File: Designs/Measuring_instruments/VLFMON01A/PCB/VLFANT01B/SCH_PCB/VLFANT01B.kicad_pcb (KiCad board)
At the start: 2 copper layers, 50.3 x 40.1 mm, 9 parts, among them J1 RJ45_RJHSE-5384, J2 RJ45_RJHSE-5384, J3 RJ45_RJHSE-5384, J7 SMA, J9 JUMP_3X2, M1 HOLE, M2 HOLE, M3 HOLE, M4 HOLE

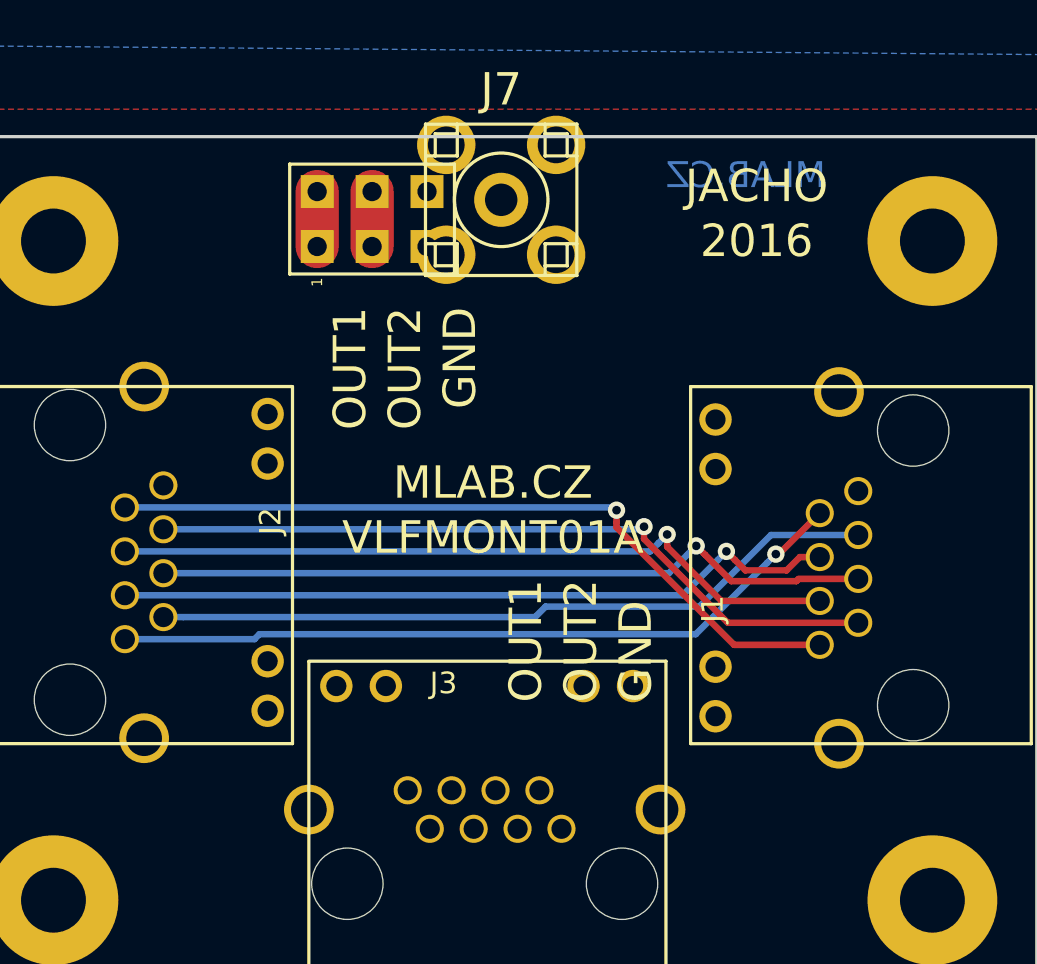
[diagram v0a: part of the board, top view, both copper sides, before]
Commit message: 
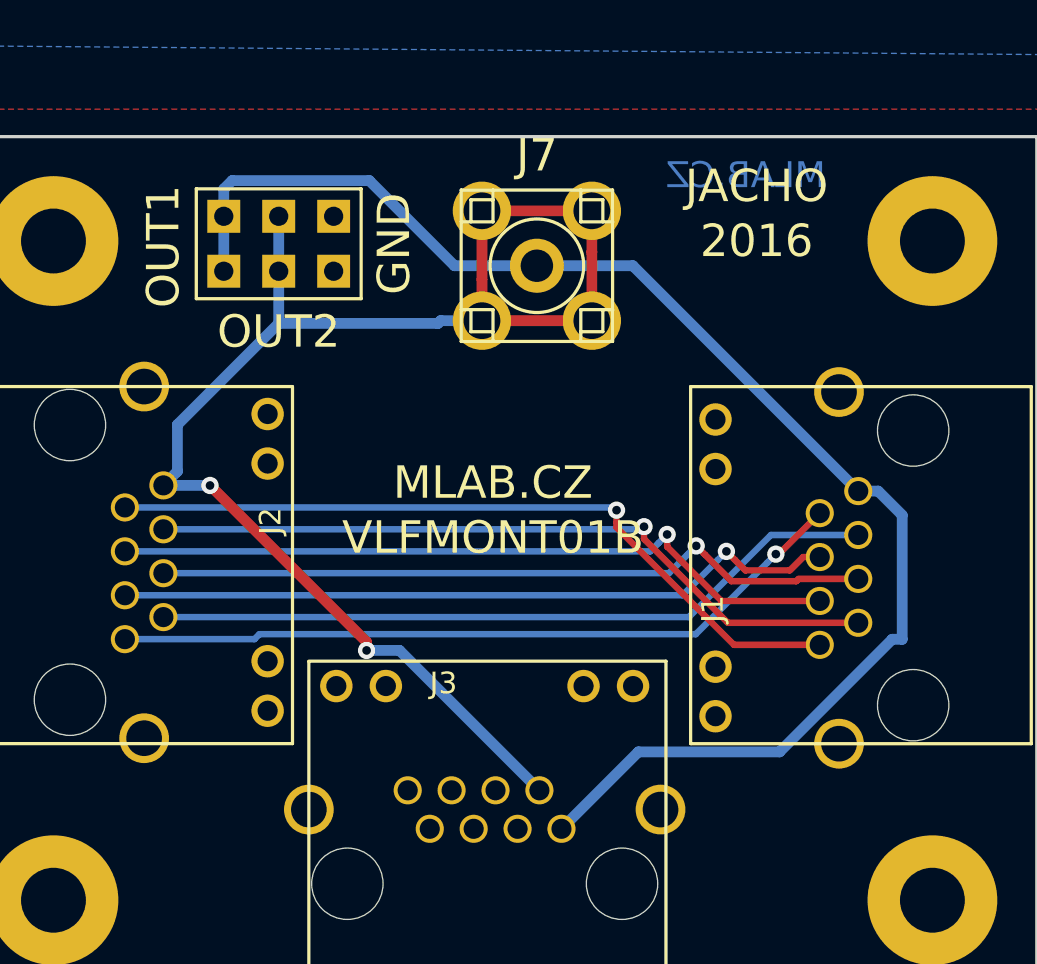
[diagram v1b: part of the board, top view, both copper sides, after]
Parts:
- moved J9 4.47 mm to (15.5, -35.4)
- moved J7 3.47 mm to (27.4, -34.4)
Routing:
- net /OUT2: track 2.54 -> 67.9 mm, vias 0 -> 2
- net /OUT1: track 2.54 -> 66.9 mm
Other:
- board text added: "VLFMONT01B"
- board text removed: "VLFMONT01A"

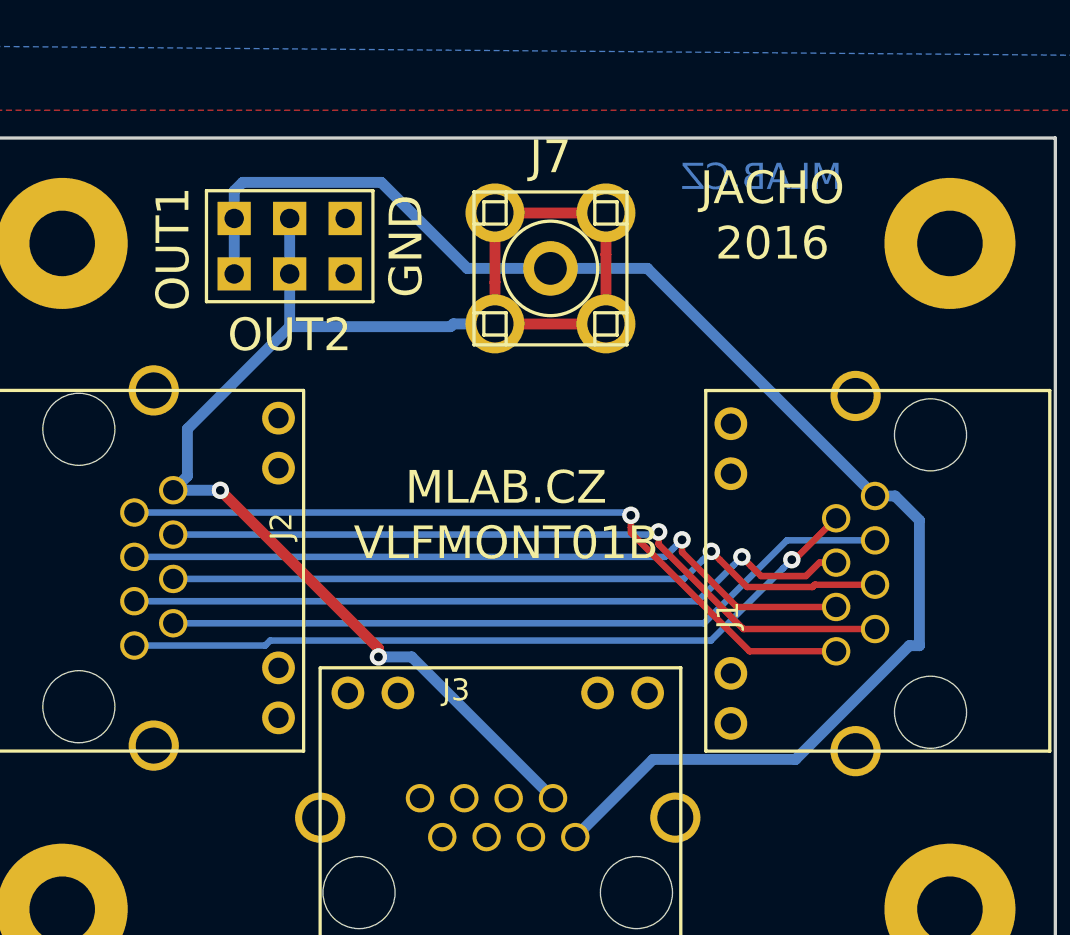
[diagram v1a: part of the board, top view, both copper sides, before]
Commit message: 
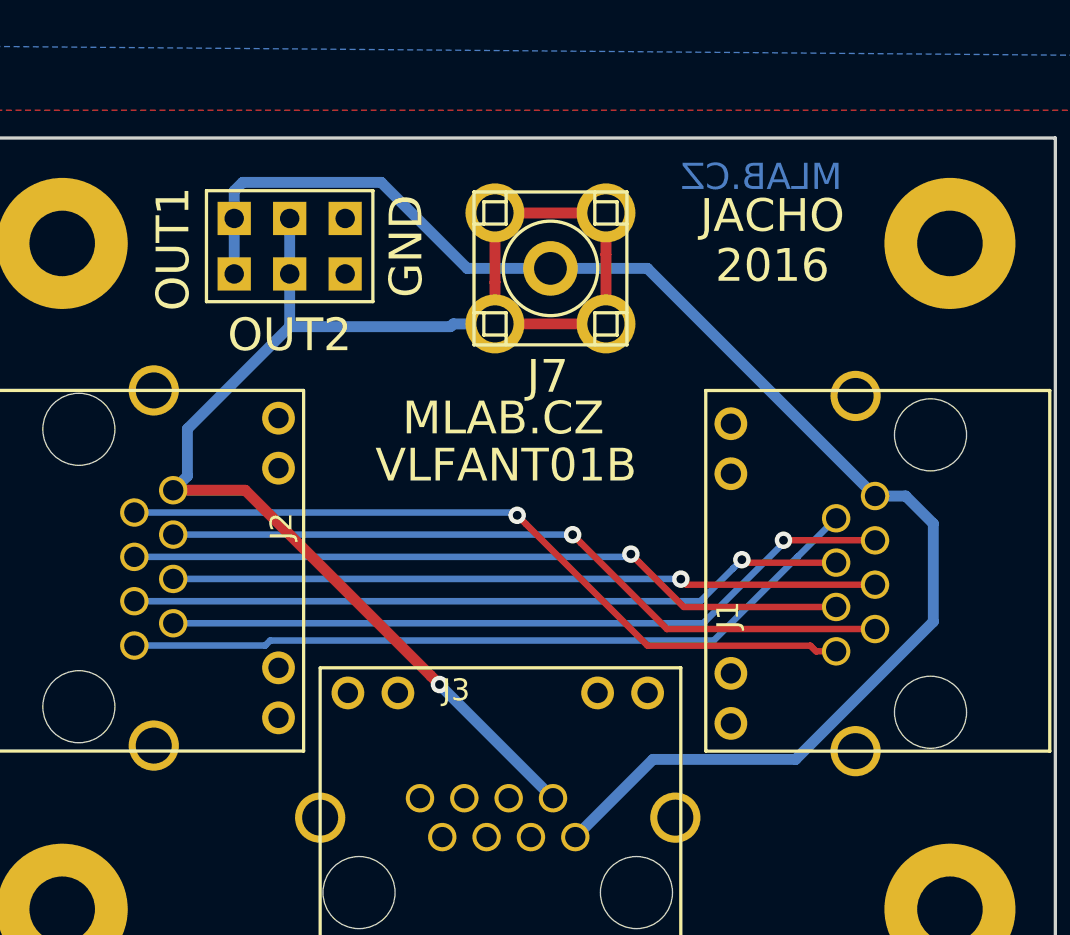
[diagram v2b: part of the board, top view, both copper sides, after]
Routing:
- net Net-(J1-Pad5): track 33.4 -> 32.2 mm
- net Net-(J1-Pad6): track 34.1 -> 33.2 mm
- net Net-(J1-Pad4): track 33.6 -> 33.0 mm
- net /OUT1: track 66.9 -> 67.4 mm
- net /OUT2: track 67.9 -> 67.7 mm, vias 2 -> 1
- net Net-(J1-Pad3): track 33.7 -> 33.8 mm, vias 0 -> 1
- net Net-(J1-Pad2): vias 1 -> 0
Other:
- board text added: "VLFANT01B"
- board text removed: "VLFMONT01B"

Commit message: zmena
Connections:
- J1 pad 10: (no net) -> Net-(J1-Pad10)
- J1 pad 11: (no net) -> Net-(J1-Pad11)
- J1 pad 12: (no net) -> Net-(J1-Pad12)
- J1 pad 9: (no net) -> Net-(J1-Pad9)
- J2 pad 10: (no net) -> Net-(J2-Pad10)
- J2 pad 11: (no net) -> Net-(J2-Pad11)
- J2 pad 12: (no net) -> Net-(J2-Pad12)
- J2 pad 9: (no net) -> Net-(J2-Pad9)
- J3 pad 1: /OUT1 -> Net-(J3-Pad1)
- J3 pad 10: (no net) -> Net-(J3-Pad10)
- J3 pad 11: (no net) -> Net-(J3-Pad11)
- J3 pad 12: (no net) -> Net-(J3-Pad12)
- J3 pad 2: /OUT2 -> Net-(J3-Pad2)
- J3 pad 3: (no net) -> Net-(J3-Pad3)
- J3 pad 4: (no net) -> /OUT1
- J3 pad 5: (no net) -> /OUT2
- J3 pad 6: (no net) -> Net-(J3-Pad6)
- J3 pad 7: (no net) -> Net-(J3-Pad7)
- J3 pad 8: (no net) -> Net-(J3-Pad8)
- J3 pad 9: (no net) -> Net-(J3-Pad9)
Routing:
- net /OUT2: track 67.7 -> 72.6 mm, vias 1 -> 0
- net /OUT1: track 67.4 -> 69.1 mm

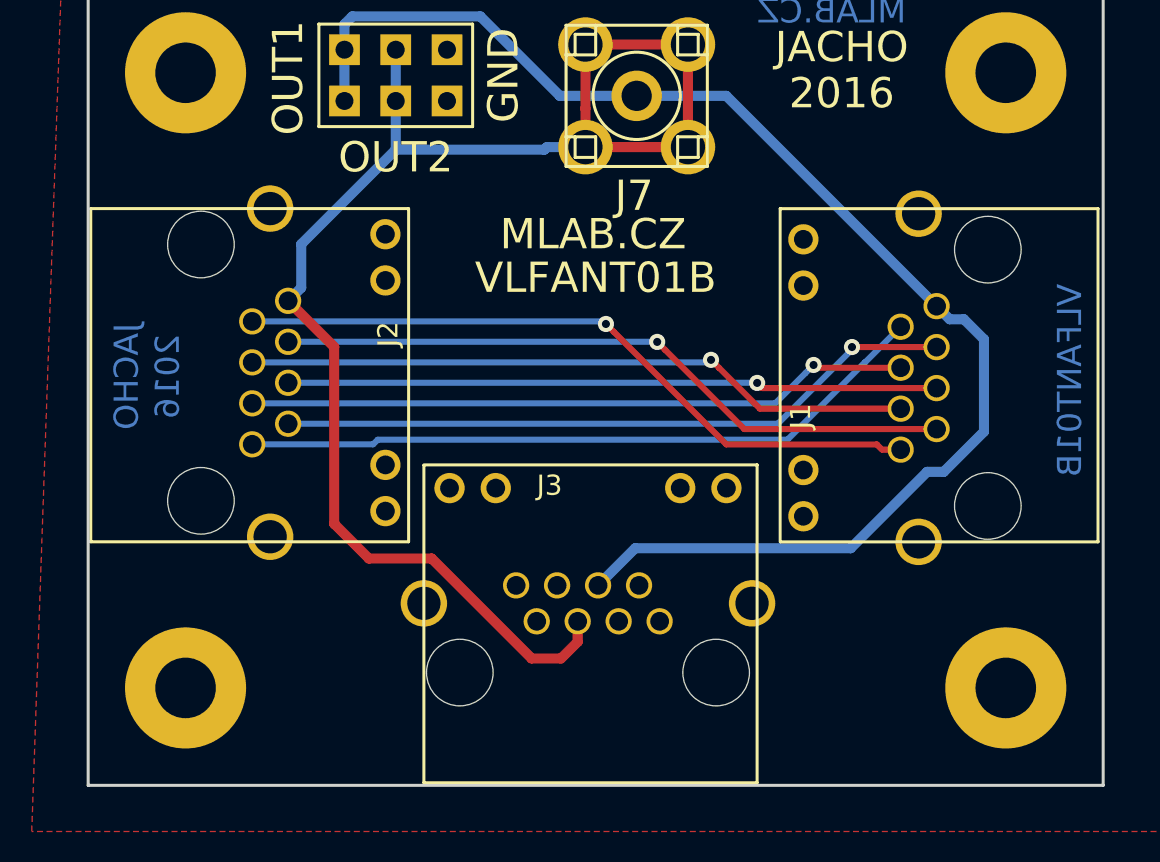
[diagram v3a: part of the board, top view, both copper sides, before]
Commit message: 
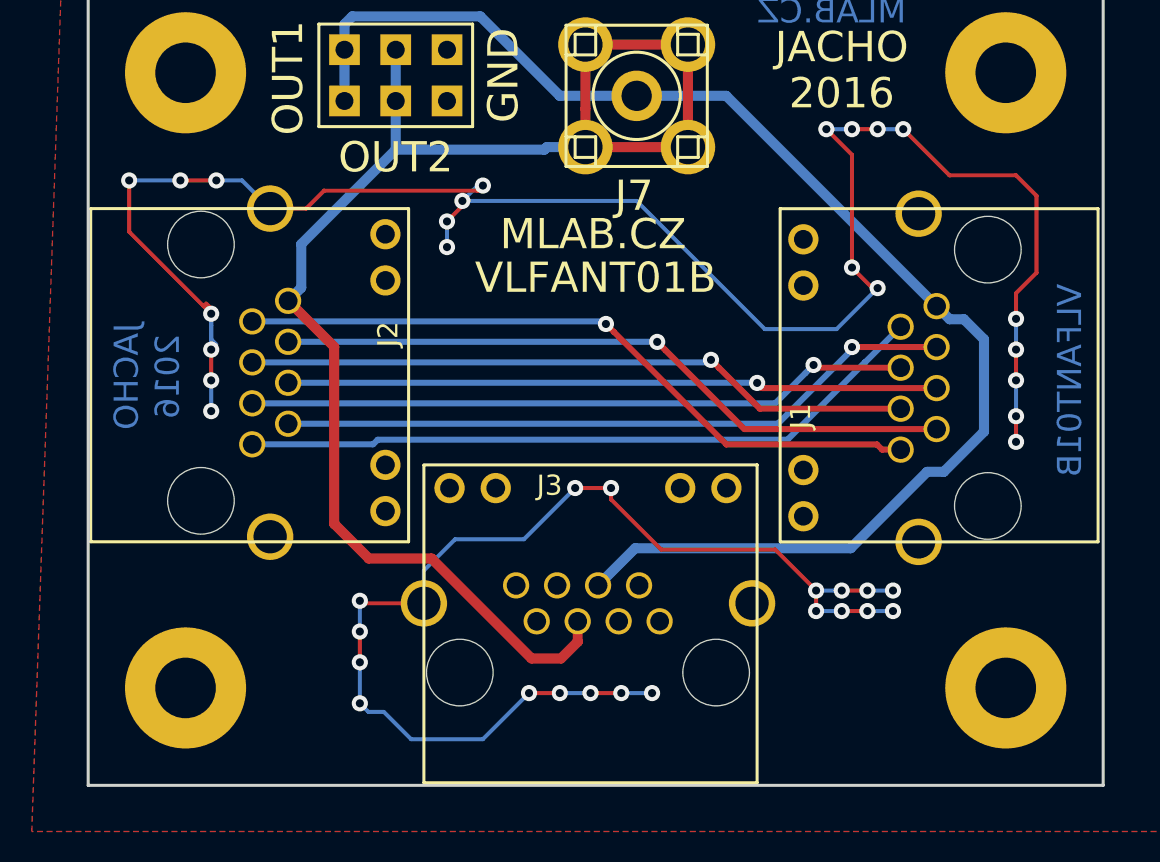
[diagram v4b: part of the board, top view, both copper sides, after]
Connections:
- J1 pad 10: Net-(J1-Pad10) -> (no net)
- J1 pad 11: Net-(J1-Pad11) -> (no net)
- J1 pad 12: Net-(J1-Pad12) -> (no net)
- J1 pad 13: GND -> (no net)
- J1 pad 9: Net-(J1-Pad9) -> (no net)
- J2 pad 10: Net-(J2-Pad10) -> (no net)
- J2 pad 11: Net-(J2-Pad11) -> (no net)
- J2 pad 12: Net-(J2-Pad12) -> (no net)
- J2 pad 9: Net-(J2-Pad9) -> (no net)
- J3 pad 1: Net-(J3-Pad1) -> (no net)
- J3 pad 10: Net-(J3-Pad10) -> (no net)
- J3 pad 11: Net-(J3-Pad11) -> (no net)
- J3 pad 12: Net-(J3-Pad12) -> (no net)
- J3 pad 2: Net-(J3-Pad2) -> (no net)
- J3 pad 3: Net-(J3-Pad3) -> (no net)
- J3 pad 6: Net-(J3-Pad6) -> (no net)
- J3 pad 7: Net-(J3-Pad7) -> (no net)
- J3 pad 8: Net-(J3-Pad8) -> (no net)
- J3 pad 9: Net-(J3-Pad9) -> (no net)
- M1 pad 1: GND -> (no net)
- M2 pad 1: GND -> (no net)
- M3 pad 1: GND -> (no net)
- M4 pad 1: GND -> (no net)
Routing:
- net GND: track 0.00 -> 153.7 mm, vias 0 -> 41

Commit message: 
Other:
- board text added: "2017"
- board text removed: "2016"
